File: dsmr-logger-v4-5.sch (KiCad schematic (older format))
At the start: 43 parts, among them J1 RJ12 female connector (6P6C), J2 Jack-DC, J3 DC-or-SM-power, J4 I2C conn, J5 Programmer, J6 Test 3v3, J7 Test 5volt, J9 ADC 0-5v, Q1 BC547, SW1 RESET, SW2 FLASH, U1 LM2937xMP, U2 4N35, U3 ESP-12E

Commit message: Add pcb layout
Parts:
- C1: footprint Capacitor_THT:CP_Radial_D5.0mm_P2.50mm -> Capacitor_THT:CP_Radial_D5.0mm_P2.00mm
- C2: footprint Capacitor_THT:CP_Radial_D6.3mm_P2.50mm -> Capacitor_THT:CP_Radial_D5.0mm_P2.00mm
- C3: footprint Capacitor_THT:CP_Radial_D10.0mm_P3.50mm -> Capacitor_THT:CP_Radial_D8.0mm_P5.00mm
- C4, C5: footprint Capacitor_THT:C_Disc_D3.0mm_W1.6mm_P2.50mm -> Capacitor_THT:C_Disc_D5.0mm_W2.5mm_P5.00mm
- D1: footprint LED_THT:LED_D5.0mm -> LED_THT:LED_D3.0mm
- J1: footprint (none) -> Connectors-P1:RJ11-6
- J2: footprint (none) -> Connector_BarrelJack:BarrelJack_CUI_PJ-102AH_Horizontal
- SW1: footprint Button_Switch_THT:SW_PUSH_6mm -> Button_Switch_THT:SW_PUSH_6mm_H7.3mm
- SW2: footprint Button_Switch_THT:SW_PUSH_6mm -> Button_Switch_THT:SW_PUSH_6mm_H13mm
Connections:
- net 3v3: now also JP2.1 (A); no longer JP1.1 (A)
- net GND: now also JP1.1 (A); no longer JP2.1 (A)
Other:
- moved on the sheet: J2, J3
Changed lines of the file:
@@
 F 0 "C1" H 2618 1596 50  0000 L CNN
 F 1 "1uF" H 2618 1505 50  0000 L CNN
-F 2 "Capacitor_THT:CP_Radial_D5.0mm_P2.50mm" H 2538 1400 50  0001 C CNN
+F 2 "Capacitor_THT:CP_Radial_D5.0mm_P2.00mm" H 2538 1400 50  0001 C CNN
 F 3 "~" H 2500 1550 50  0001 C CNN
 	1    2500 1550
@@
 F 0 "C2" H 3568 1596 50  0000 L CNN
 F 1 "2.2uF" H 3568 1505 50  0000 L CNN
-F 2 "Capacitor_THT:CP_Radial_D6.3mm_P2.50mm" H 3488 1400 50  0001 C CNN
+F 2 "Capacitor_THT:CP_Radial_D5.0mm_P2.00mm" H 3488 1400 50  0001 C CNN
 F 3 "~" H 3450 1550 50  0001 C CNN
 	1    3450 1550
@@
 F 0 "C3" H 4068 1596 50  0000 L CNN
 F 1 "200-1000uF" H 4068 1505 50  0000 L CNN
-F 2 "Capacitor_THT:CP_Radial_D10.0mm_P3.50mm" H 3988 1400 50  0001 C CNN
+F 2 "Capacitor_THT:CP_Radial_D8.0mm_P5.00mm" H 3988 1400 50  0001 C CNN
 F 3 "~" H 3950 1550 50  0001 C CNN
 	1    3950 1550
@@
 	1    0    0    -1
 $EndComp
-Text GLabel 7300 1700 0    50   Input ~ 0
+Text GLabel 7300 1700 0    50   UnSpc ~ 0
+GND
+Text GLabel 7300 1800 0    50   Input ~ 0
 3v3
-Text GLabel 7300 1800 0    50   UnSpc ~ 0
-GND
 Text GLabel 7300 1900 0    50   Input ~ 0
 SCL
@@
 F 0 "J1" H 2607 3967 50  0000 C CNN
 F 1 "RJ12 female connector (6P6C)" H 2607 3876 50  0000 C CNN
-F 2 "" V 2550 3425 50  0001 C CNN
+F 2 "Connectors-P1:RJ11-6" V 2550 3425 50  0001 C CNN
 F 3 "~" V 2550 3425 50  0001 C CNN
 	1    2550 3400
@@
 F 0 "C4" H 9515 3146 50  0000 L CNN
 F 1 "100nF" H 9515 3055 50  0000 L CNN
-F 2 "Capacitor_THT:C_Disc_D3.0mm_W1.6mm_P2.50mm" H 9438 2950 50  0001 C CNN
+F 2 "Capacitor_THT:C_Disc_D5.0mm_W2.5mm_P5.00mm" H 9438 2950 50  0001 C CNN
 F 3 "~" H 9400 3100 50  0001 C CNN
 	1    9400 3100
@@
 F 0 "D1" V 1239 6332 50  0000 R CNN
 F 1 "PWR LED" V 1148 6332 50  0000 R CNN
-F 2 "LED_THT:LED_D5.0mm" H 1200 6450 50  0001 C CNN
+F 2 "LED_THT:LED_D3.0mm" H 1200 6450 50  0001 C CNN
 F 3 "~" H 1200 6450 50  0001 C CNN
 	1    1200 6450
@@
 F 0 "C5" H 2515 6996 50  0000 L CNN
 F 1 "100nF" H 2515 6905 50  0000 L CNN
-F 2 "Capacitor_THT:C_Disc_D3.0mm_W1.6mm_P2.50mm" H 2438 6800 50  0001 C CNN
+F 2 "Capacitor_THT:C_Disc_D5.0mm_W2.5mm_P5.00mm" H 2438 6800 50  0001 C CNN
 F 3 "~" H 2400 6950 50  0001 C CNN
 	1    2400 6950
@@
 F 0 "SW1" H 2150 6985 50  0000 C CNN
 F 1 "RESET" H 2150 6894 50  0000 C CNN
-F 2 "Button_Switch_THT:SW_PUSH_6mm" H 2150 6900 50  0001 C CNN
+F 2 "Button_Switch_THT:SW_PUSH_6mm_H7.3mm" H 2150 6900 50  0001 C CNN
 F 3 "~" H 2150 6900 50  0001 C CNN
 	1    2150 6700
@@
 F 0 "SW2" H 3550 6985 50  0000 C CNN
 F 1 "FLASH" H 3550 6894 50  0000 C CNN
-F 2 "Button_Switch_THT:SW_PUSH_6mm" H 3550 6900 50  0001 C CNN
+F 2 "Button_Switch_THT:SW_PUSH_6mm_H13mm" H 3550 6900 50  0001 C CNN
 F 3 "~" H 3550 6900 50  0001 C CNN
 	1    3550 6700
@@
 L Connector:Jack-DC J2
 U 1 1 5E112C34
-P 1600 4800
-F 0 "J2" H 1657 5125 50  0000 C CNN
-F 1 "Jack-DC" H 1657 5034 50  0000 C CNN
-F 2 "" H 1650 4760 50  0001 C CNN
-F 3 "~" H 1650 4760 50  0001 C CNN
-	1    1600 4800
+P 1400 4950
+F 0 "J2" H 1457 5275 50  0000 C CNN
+F 1 "Jack-DC" H 1457 5184 50  0000 C CNN
+F 2 "Connector_BarrelJack:BarrelJack_CUI_PJ-102AH_Horizontal" H 1450 4910 50  0001 C CNN
+F 3 "~" H 1450 4910 50  0001 C CNN
+	1    1400 4950
 	1    0    0    -1
 $EndComp
@@
 L Connector:Conn_01x03_Male J3
 U 1 1 5E113AD6
-P 3000 4800
-F 0 "J3" H 2972 4732 50  0000 R CNN
-F 1 "DC-or-SM-power" H 2972 4823 50  0000 R CNN
-F 2 "Connector_PinHeader_2.54mm:PinHeader_1x03_P2.54mm_Vertical" H 3000 4800 50  0001 C CNN
-F 3 "~" H 3000 4800 50  0001 C CNN
-	1    3000 4800
+P 2800 4950
+F 0 "J3" H 2772 4882 50  0000 R CNN
+F 1 "DC-or-SM-power" H 2772 4973 50  0000 R CNN
+F 2 "Connector_PinHeader_2.54mm:PinHeader_1x03_P2.54mm_Vertical" H 2800 4950 50  0001 C CNN
+F 3 "~" H 2800 4950 50  0001 C CNN
+	1    2800 4950
 	-1   0    0    1
 $EndComp
@@
 L power:GND #PWR0114
 U 1 1 5E118460
-P 2000 5100
-F 0 "#PWR0114" H 2000 4850 50  0001 C CNN
-F 1 "GND" H 2005 4927 50  0000 C CNN
-F 2 "" H 2000 5100 50  0001 C CNN
-F 3 "" H 2000 5100 50  0001 C CNN
-	1    2000 5100
-	1    0    0    -1
-$EndComp
-Text GLabel 2550 4900 0    50   Input ~ 0
+P 1800 5250
+F 0 "#PWR0114" H 1800 5000 50  0001 C CNN
+F 1 "GND" H 1805 5077 50  0000 C CNN
+F 2 "" H 1800 5250 50  0001 C CNN
+F 3 "" H 1800 5250 50  0001 C CNN
+	1    1800 5250
+	1    0    0    -1
+$EndComp
+Text GLabel 2350 5050 0    50   Input ~ 0
 5Volt_SM
 Wire Wire Line
-	2550 4900 2800 4900
-Wire Wire Line
-	1900 4700 2800 4700
-Text GLabel 2550 4800 0    50   Output ~ 0
+	2350 5050 2600 5050
+Wire Wire Line
+	1700 4850 2600 4850
+Text GLabel 2350 4950 0    50   Output ~ 0
 5Volt
 $Comp
@@
 $EndComp
 Wire Wire Line
-	1900 4900 2000 4900
-Wire Wire Line
-	2000 4900 2000 5100
-Wire Wire Line
-	2550 4800 2800 4800
+	1700 5050 1800 5050
+Wire Wire Line
+	1800 5050 1800 5250
+Wire Wire Line
+	2350 4950 2600 4950
+Wire Notes Line
+	3800 4450 900  4450
+Wire Notes Line
+	900  4450 900  5550
+Wire Notes Line
+	900  5550 3800 5550
+Wire Notes Line
+	3800 5550 3800 4450
 $EndSCHEMATC

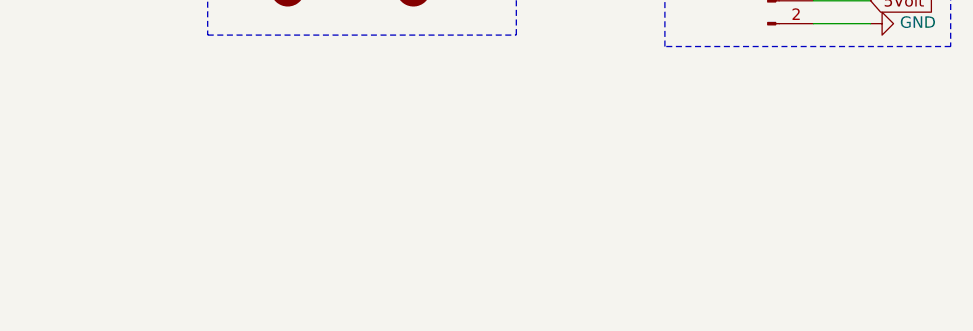
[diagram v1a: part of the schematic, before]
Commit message: Silk mask updated, changed JP4, added 3D renders
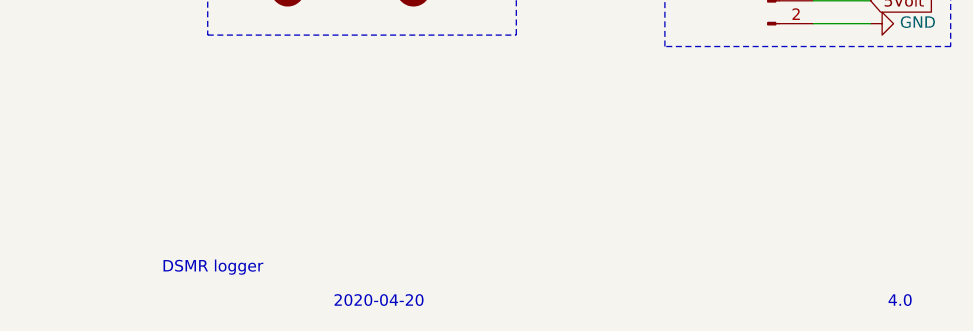
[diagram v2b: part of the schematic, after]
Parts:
- J4: footprint Connector_PinHeader_2.54mm:PinHeader_1x04_P2.54mm_Vertical -> Connector_PinSocket_2.54mm:PinSocket_1x04_P2.54mm_Vertical
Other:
- note added: "2020-04-20"
- note added: "4.0"
- note added: "DSMR logger"
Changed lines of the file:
@@
 F 0 "J4" H 8722 1782 50  0000 R CNN
 F 1 "I2C conn" H 8722 1873 50  0000 R CNN
-F 2 "Connector_PinHeader_2.54mm:PinHeader_1x04_P2.54mm_Vertical" H 8750 1900 50  0001 C CNN
+F 2 "Connector_PinSocket_2.54mm:PinSocket_1x04_P2.54mm_Vertical" H 8750 1900 50  0001 C CNN
 F 3 "~" H 8750 1900 50  0001 C CNN
 	1    8750 1900
@@
 Wire Notes Line
 	3800 5550 3800 4450
+Text Notes 7400 7500 0    50   ~ 0
+DSMR logger
+Text Notes 10575 7650 0    50   ~ 0
+4.0
+Text Notes 8150 7650 0    50   ~ 0
+2020-04-20
 $EndSCHEMATC
